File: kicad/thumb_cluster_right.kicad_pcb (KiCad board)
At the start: 2 copper layers, 41.2 x 46.6 mm, 18 parts, among them J1 Conn_01x07

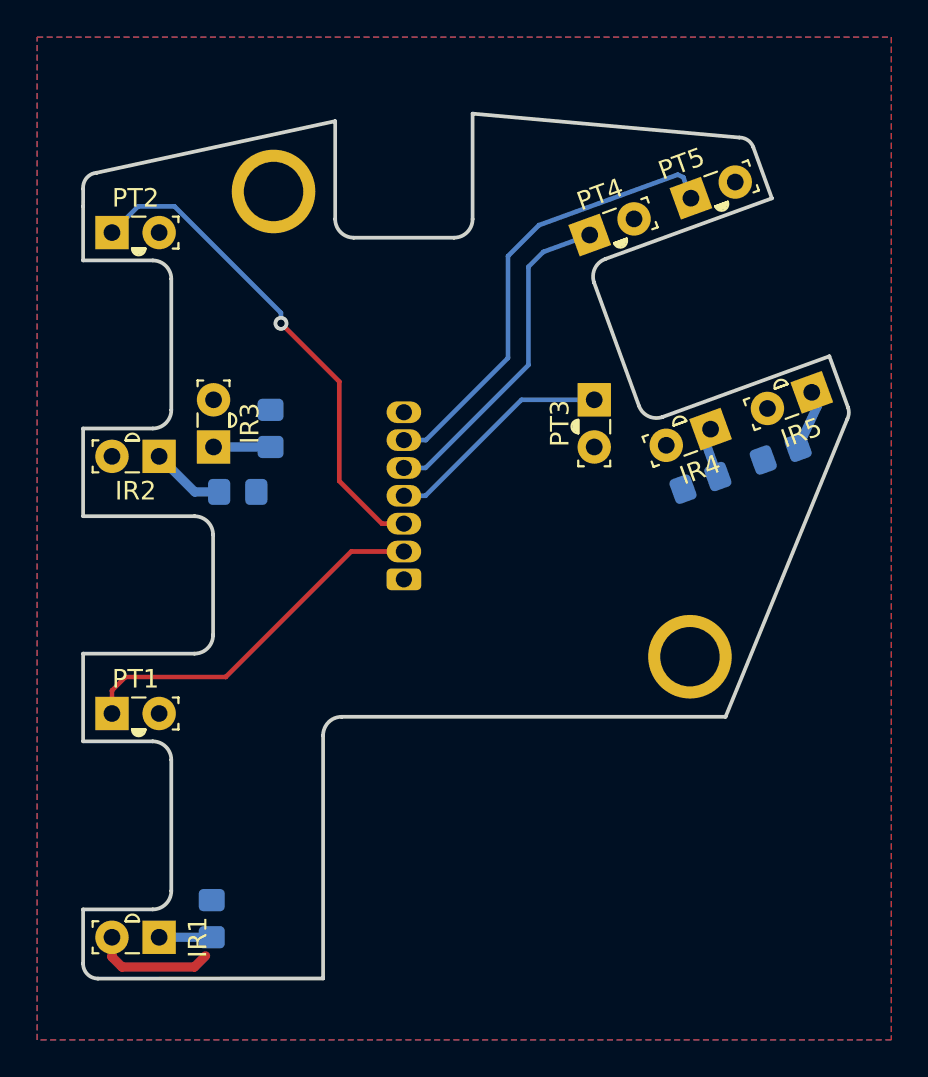
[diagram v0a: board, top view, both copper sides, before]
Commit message: Initial commit of lalboard extended features, including breakout board.
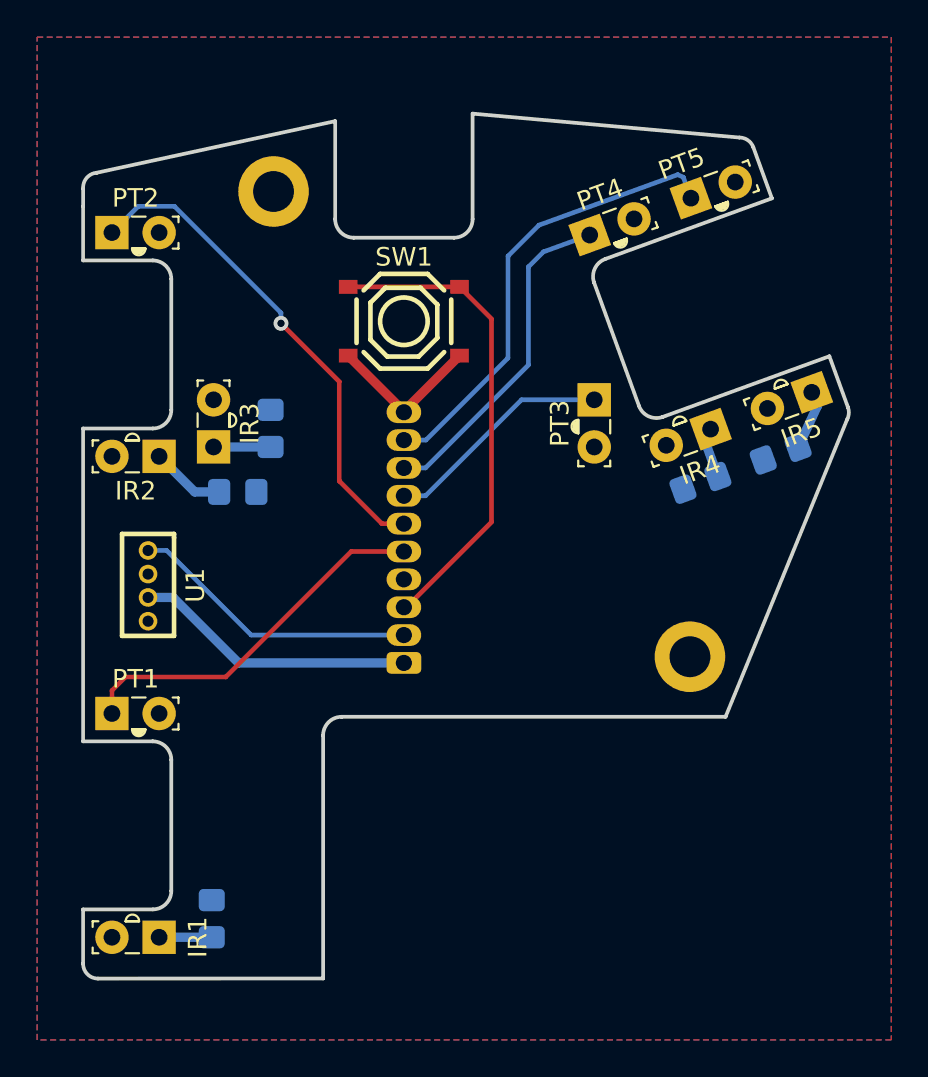
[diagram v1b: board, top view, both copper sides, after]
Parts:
- added SW1: TS-1187A-B-A-B, easyeda2kicad:SW-SMD_4P-L5.1-W5.1-P3.70-LS6.5-TL_H1.5, F.Cu at (142.8, 73.3)
- added U1: WS2812D-255, easyeda2kicad:LED-TH_4P-L5.0-W2.5-P1.27_WS2812D-255, F.Cu at (129.0, 87.5)
- H1, H2: footprint MountingHole:MountingHole_3.2mm_M3_Pad -> MountingHole:MountingHole_2.2mm_M2_DIN965_Pad
- J1: footprint lalboard:JST_ZH_B7B-ZR_1x07_P1.50mm_Vertical -> Connector_Wuerth:Wuerth_WR-WTB_64801011622_1x10_P1.50mm_Vertical
- moved J1 4.50 mm to (142.8, 91.7)
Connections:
- J1 pad 1: +3.3V -> +5V
- J1 pad 2: C1 -> C7
- J1 pad 3: C2 -> C6
- J1 pad 4: C3 -> +3.3V
- J1 pad 5: C4 -> C1
- J1 pad 6: C5 -> C2
- J1 pad 7: GND -> C3
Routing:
- net C6: track 0.00 -> 26.0 mm
- net C7: track 0.00 -> 15.7 mm
- net +5V: track 0.00 -> 15.2 mm
- net GND: track 0.00 -> 8.62 mm
- net +3.3V: track 6.57 -> 0.00 mm
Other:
- outline, holes or cut-outs redrawn
- board text added: "lalboard-extended right thumb cluster v2.6.0"
- board text removed: "lalboard.com right thumb cluster v2.5.0"
